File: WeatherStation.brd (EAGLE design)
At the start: 30.5 x 53.3 mm, 36 parts, among them J1 EDISON_CONNECTOR_FULLMOUNTING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, J2 EDISON_CONNECTOR_FULLHEADER, U1 MCP73831, U2 HTU21DSMD, U3 MPL3115A2LGA8, U4 PCA9306

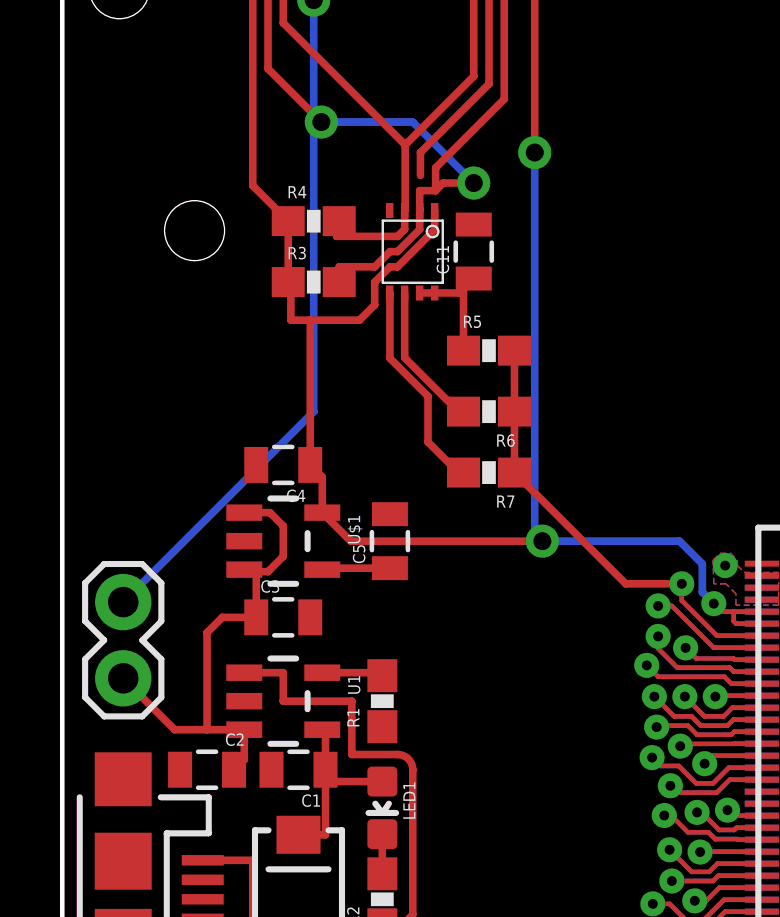
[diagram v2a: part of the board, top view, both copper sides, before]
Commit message: rearranged silkscreens
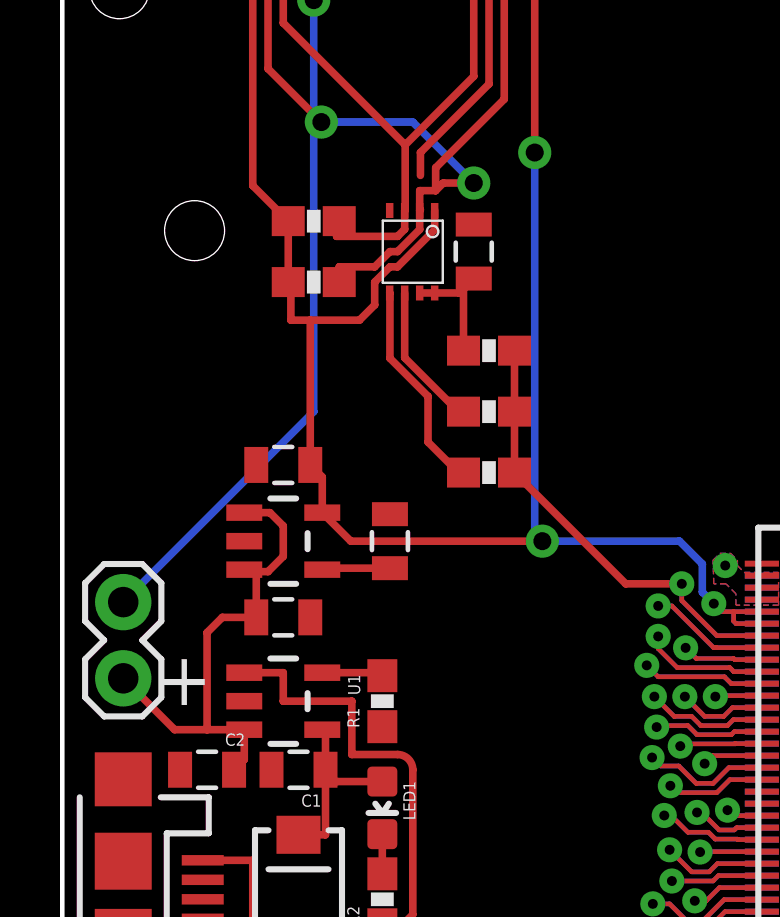
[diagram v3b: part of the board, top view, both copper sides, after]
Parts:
- U$1: value 3.3V/150mA -> MIC5205
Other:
- board text added: "+"
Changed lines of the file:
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@@
 <wire x1="11.176" y1="50.546" x2="11.176" y2="46.482" width="2.54" layer="46"/>
 <wire x1="11.176" y1="46.482" x2="9.398" y2="44.704" width="2.54" layer="46"/>
+<text x="4.064" y="19.558" size="1.778" layer="25" align="center">+</text>
 </plain>
 <attributes>
@@
 <attribute name="PROD_ID" value="IC-10023" x="11.684" y="33.782" size="1.778" layer="27" rot="R180" display="off"/>
 </element>
-<element name="U$1" library="SparkFun-PowerIC" package="SOT23-5" value="3.3V/150mA" x="7.366" y="24.13" rot="R270">
+<element name="U$1" library="SparkFun-PowerIC" package="SOT23-5" value="MIC5205" x="7.366" y="24.13" smashed="yes" rot="R270">
 <attribute name="PROD_ID" value="VREG-00822" x="7.366" y="24.13" size="1.778" layer="27" rot="R270" display="off"/>
-</element>
-<element name="C3" library="SparkFun-Capacitors" package="0805" value="4.7µF" x="7.366" y="21.59"/>
-<element name="C4" library="SparkFun-Capacitors" package="0805" value="4.7µF" x="7.366" y="26.67" rot="R180"/>
-<element name="C5" library="SparkFun-Capacitors" package="0805" value="4.7µF" x="10.922" y="24.13" rot="R90"/>
+<attribute name="VALUE" x="7.3025" y="24.1935" size="0.4064" layer="27" rot="R90" align="center"/>
+</element>
+<element name="C3" library="SparkFun-Capacitors" package="0805" value="4.7µF" x="7.366" y="21.59" smashed="yes">
+<attribute name="VALUE" x="8.89" y="21.463" size="0.4064" layer="27"/>
+</element>
+<element name="C4" library="SparkFun-Capacitors" package="0805" value="4.7µF" x="7.366" y="26.67" smashed="yes" rot="R180">
+<attribute name="VALUE" x="8.382" y="28.067" size="0.4064" layer="27" rot="R180"/>
+</element>
+<element name="C5" library="SparkFun-Capacitors" package="0805" value="4.7µF" x="10.922" y="24.13" smashed="yes" rot="R90">
+<attribute name="VALUE" x="12.319" y="23.114" size="0.4064" layer="27" rot="R90"/>
+</element>
 <element name="C6" library="SparkFun-Capacitors" package="0805" value="0.1µF" x="21.336" y="48.514" rot="R90"/>
 <element name="C7" library="SparkFun-Capacitors" package="0805" value="1µF" x="22.86" y="48.514" rot="R90"/>
-<element name="R3" library="SparkFun-Resistors" package="0603-RES" value="1kΩ" x="8.382" y="32.766"/>
-<element name="R4" library="SparkFun-Resistors" package="0603-RES" value="1kΩ" x="8.382" y="34.798"/>
-<element name="R5" library="SparkFun-Resistors" package="0603-RES" value="1kΩ" x="14.224" y="30.48"/>
-<element name="R6" library="SparkFun-Resistors" package="0603-RES" value="1kΩ" x="14.224" y="28.448" rot="R180"/>
-<element name="R7" library="SparkFun-Resistors" package="0603-RES" value="1kΩ" x="14.224" y="26.416" rot="R180"/>
+<element name="R3" library="SparkFun-Resistors" package="0603-RES" value="1kΩ" x="8.382" y="32.766" smashed="yes">
+<attribute name="VALUE" x="5.842" y="32.639" size="0.4064" layer="27"/>
+</element>
+<element name="R4" library="SparkFun-Resistors" package="0603-RES" value="1kΩ" x="8.382" y="34.798" smashed="yes">
+<attribute name="VALUE" x="5.842" y="34.671" size="0.4064" layer="27"/>
+</element>
+<element name="R5" library="SparkFun-Resistors" package="0603-RES" value="1kΩ" x="14.224" y="30.48" smashed="yes">
+<attribute name="VALUE" x="11.684" y="30.353" size="0.4064" layer="27"/>
+</element>
+<element name="R6" library="SparkFun-Resistors" package="0603-RES" value="1kΩ" x="14.224" y="28.448" smashed="yes" rot="R180">
+<attribute name="VALUE" x="11.684" y="28.321" size="0.4064" layer="27" rot="R180" align="top-right"/>
+</element>
+<element name="R7" library="SparkFun-Resistors" package="0603-RES" value="1kΩ" x="14.224" y="26.416" smashed="yes" rot="R180">
+<attribute name="VALUE" x="11.684" y="26.289" size="0.4064" layer="27"/>
+</element>
 <element name="C8" library="SparkFun-Capacitors" package="0805" value="4.7µF" x="7.112" y="51.562"/>
 <element name="C9" library="SparkFun-Capacitors" package="0805" value="0.1µF" x="17.78" y="45.72"/>
 <element name="C10" library="SparkFun-Capacitors" package="EIA3216" value="10µF" x="25.146" y="48.514" rot="R270"/>
-<element name="C11" library="SparkFun-Capacitors" package="0805" value="4.7µF" x="13.716" y="33.782" rot="R90"/>
+<element name="C11" library="SparkFun-Capacitors" package="0805" value="4.7µF" x="13.716" y="33.782" smashed="yes" rot="R90">
+<attribute name="VALUE" x="15.113" y="32.766" size="0.4064" layer="27" rot="R90"/>
+</element>
 </elements>
 <signals>

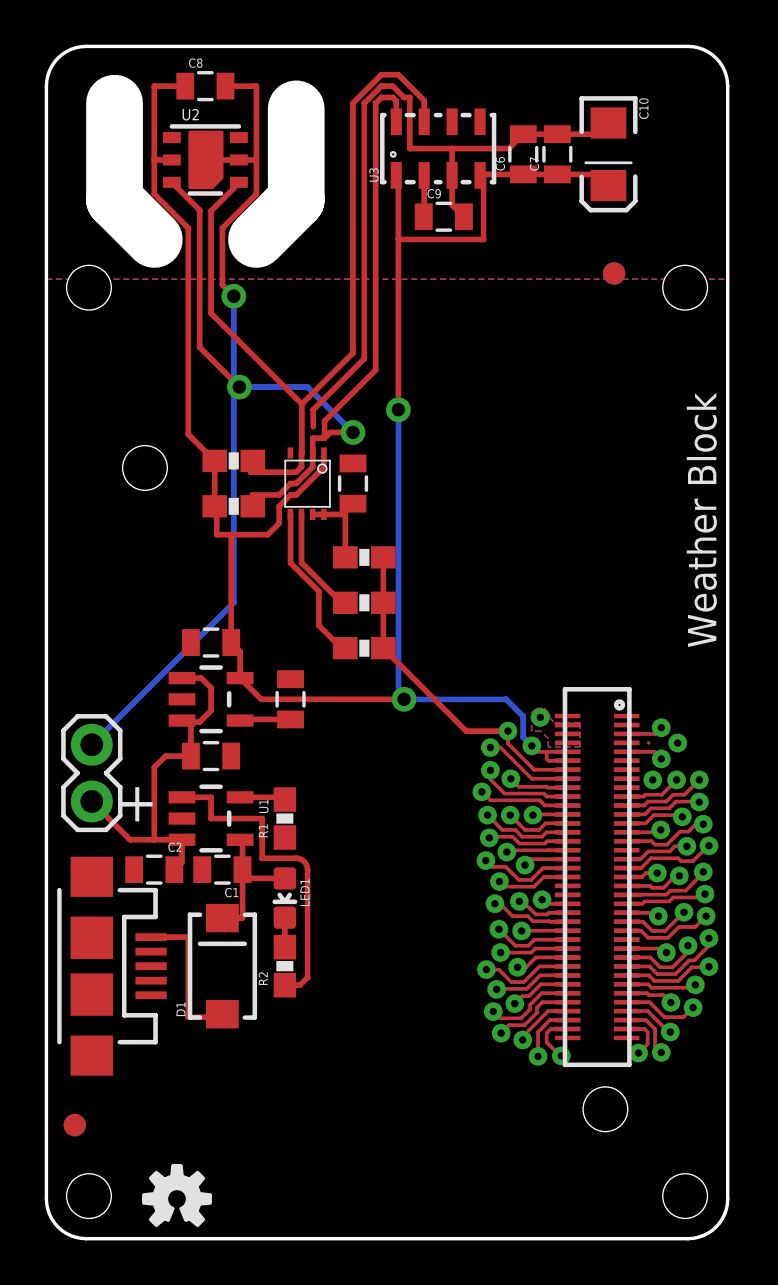
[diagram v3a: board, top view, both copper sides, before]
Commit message: rearranged silkscreens/labels
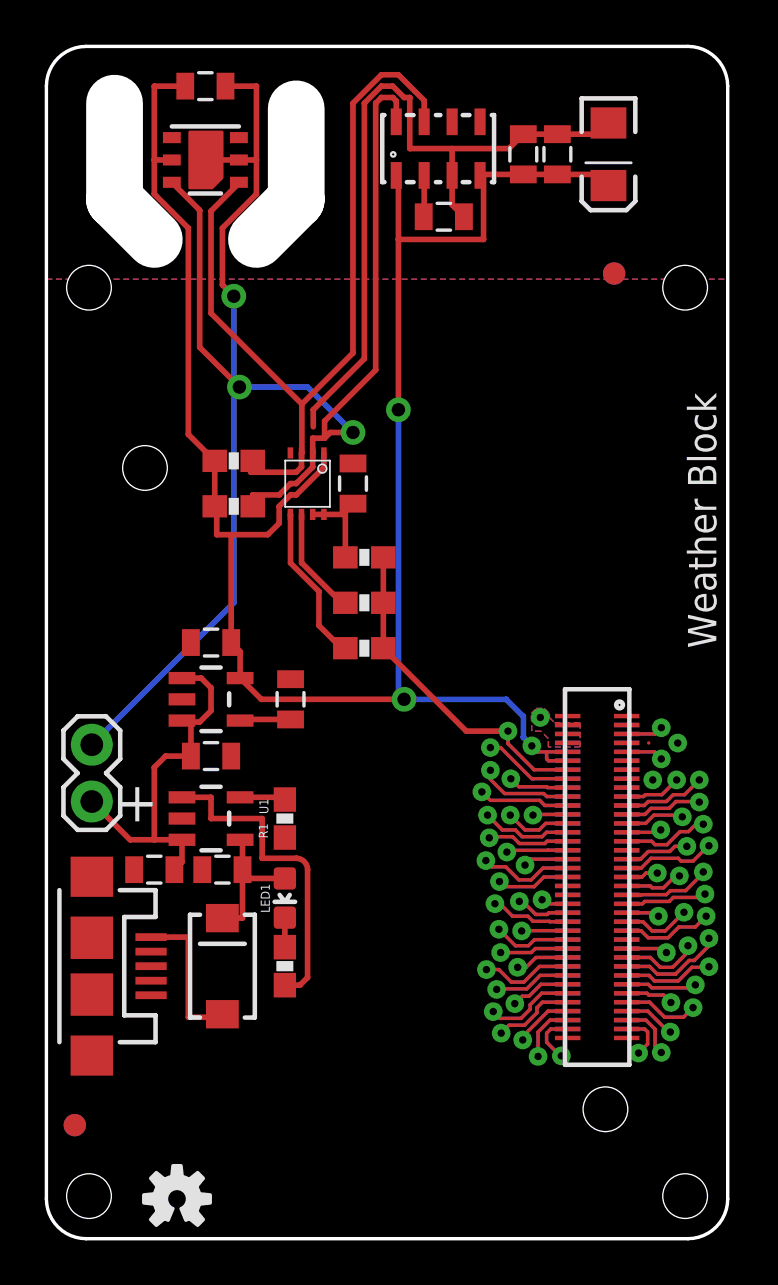
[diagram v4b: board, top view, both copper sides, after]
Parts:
- U2: value HTU21DSMD -> HTU21D
- U3: value MPL3115A2LGA8 -> MPL3115A2
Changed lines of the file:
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@@
 <dimension x1="1.778" y1="44.45" x2="5.08" y2="0" x3="38.1" y3="22.225" textsize="1.27" textratio="10" layer="51" dtype="vertical" unit="inch"/>
 <dimension x1="0" y1="53.34" x2="2.54" y2="0" x3="40.64" y3="26.67" textsize="1.27" textratio="10" layer="51" dtype="vertical" unit="inch"/>
-<rectangle x1="22.098" y1="26.162" x2="30.48" y2="44.45" layer="42" rot="R180"/>
 <rectangle x1="22.098" y1="26.162" x2="30.48" y2="44.45" layer="41" rot="R180"/>
 <dimension x1="1.905" y1="42.545" x2="0.5579625" y2="43.8920375" x3="-5.07986875" y3="49.285071875" textsize="1.27" textratio="10" layer="51" dtype="radius" unit="inch"/>
@@
 <attribute name="PROD_ID" value="CONN-09505" x="2.032" y="12.192" size="1.778" layer="27" rot="R270" display="off"/>
 </element>
-<element name="D1" library="SparkFun-DiscreteSemi" package="SMA-DIODE" value="MBRA140" x="7.874" y="12.192" rot="R90">
+<element name="D1" library="SparkFun-DiscreteSemi" package="SMA-DIODE" value="MBRA140" x="7.874" y="12.192" smashed="yes" rot="R90">
 <attribute name="PROD_ID" value="DIO-08053" x="7.874" y="12.192" size="1.778" layer="27" rot="R90" display="off"/>
 </element>
@@
 <attribute name="VALUE" x="7.4295" y="18.7325" size="0.3048" layer="27" rot="R270" align="center"/>
 </element>
-<element name="C1" library="SparkFun-Capacitors" package="0805" value="4.7µF" x="7.874" y="16.51" smashed="yes" rot="R180">
-<attribute name="NAME" x="8.636" y="15.6845" size="0.4064" layer="25" rot="R180"/>
-</element>
+<element name="C1" library="SparkFun-Capacitors" package="0805" value="4.7µF" x="7.874" y="16.51" smashed="yes" rot="R180"/>
 <element name="R1" library="SparkFun-Resistors" package="0603-RES" value="2kΩ" x="10.668" y="18.796" rot="R90"/>
 <element name="C2" library="SparkFun-Capacitors" package="0805" value="4.7µF" x="4.826" y="16.51" smashed="yes" rot="R180">
-<attribute name="NAME" x="6.096" y="17.7165" size="0.4064" layer="25" rot="R180"/>
-</element>
-<element name="LED1" library="SparkFun-LED" package="LED-0603" value="" x="10.668" y="15.24" rot="R180"/>
-<element name="R2" library="SparkFun-Resistors" package="0603-RES" value="330Ω" x="10.668" y="12.192" rot="R90"/>
+<attribute name="VALUE" x="7.112" y="15.621" size="0.4064" layer="27" rot="R180"/>
+</element>
+<element name="LED1" library="SparkFun-LED" package="LED-0603" value="" x="10.668" y="15.24" smashed="yes" rot="R180">
+<attribute name="NAME" x="9.5885" y="15.875" size="0.4064" layer="25" rot="R270"/>
+<attribute name="VALUE" x="9.5885" y="16.256" size="0.4064" layer="27" rot="R270"/>
+</element>
+<element name="R2" library="SparkFun-Resistors" package="0603-RES" value="330Ω" x="10.668" y="12.192" smashed="yes" rot="R90">
+<attribute name="VALUE" x="9.779" y="12.192" size="0.4064" layer="27" rot="R90" align="center"/>
+</element>
 <element name="JP2" library="SparkFun-Connectors" package="1X02" value="M02PTH" x="2.032" y="22.098" smashed="yes" rot="R270"/>
-<element name="U2" library="SparkFun-Sensors" package="HTU21D" value="HTU21DSMD" x="7.112" y="48.26"/>
-<element name="U3" library="SparkFun-Sensors" package="LGA8" value="MPL3115A2LGA8" x="17.526" y="48.768" rot="R90"/>
+<element name="U2" library="SparkFun-Sensors" package="HTU21D" value="HTU21D" x="7.112" y="48.26" smashed="yes">
+<attribute name="VALUE" x="5.787" y="46.06" size="0.5" layer="27"/>
+</element>
+<element name="U3" library="SparkFun-Sensors" package="LGA8" value="MPL3115A2" x="17.526" y="48.768" smashed="yes" rot="R90">
+<attribute name="VALUE" x="16.002" y="50.8" size="0.4064" layer="27" ratio="15"/>
+</element>
 <element name="U4" library="SparkFun-DigitalIC" package="PSOP-8" value="PCA9306" x="11.684" y="33.782" rot="R180">
 <attribute name="PROD_ID" value="IC-10023" x="11.684" y="33.782" size="1.778" layer="27" rot="R180" display="off"/>
@@
 </element>
 <element name="C5" library="SparkFun-Capacitors" package="0805" value="4.7µF" x="10.922" y="24.13" smashed="yes" rot="R90">
-<attribute name="VALUE" x="12.319" y="23.114" size="0.4064" layer="27" rot="R90"/>
-</element>
-<element name="C6" library="SparkFun-Capacitors" package="0805" value="0.1µF" x="21.336" y="48.514" rot="R90"/>
-<element name="C7" library="SparkFun-Capacitors" package="0805" value="1µF" x="22.86" y="48.514" rot="R90"/>
+<attribute name="VALUE" x="11.811" y="24.13" size="0.4064" layer="27" rot="R90" align="top-center"/>
+</element>
+<element name="C6" library="SparkFun-Capacitors" package="0805" value="0.1µF" x="21.336" y="48.514" smashed="yes" rot="R90">
+<attribute name="VALUE" x="21.463" y="46.99" size="0.4064" layer="27" rot="R90" align="bottom-right"/>
+</element>
+<element name="C7" library="SparkFun-Capacitors" package="0805" value="1µF" x="22.86" y="48.514" smashed="yes" rot="R90">
+<attribute name="VALUE" x="22.987" y="46.99" size="0.4064" layer="27" rot="R90" align="bottom-right"/>
+</element>
 <element name="R3" library="SparkFun-Resistors" package="0603-RES" value="1kΩ" x="8.382" y="32.766" smashed="yes">
 <attribute name="VALUE" x="5.842" y="32.639" size="0.4064" layer="27"/>
@@
 <attribute name="VALUE" x="11.684" y="26.289" size="0.4064" layer="27"/>
 </element>
-<element name="C8" library="SparkFun-Capacitors" package="0805" value="4.7µF" x="7.112" y="51.562"/>
-<element name="C9" library="SparkFun-Capacitors" package="0805" value="0.1µF" x="17.78" y="45.72"/>
-<element name="C10" library="SparkFun-Capacitors" package="EIA3216" value="10µF" x="25.146" y="48.514" rot="R270"/>
+<element name="C8" library="SparkFun-Capacitors" package="0805" value="4.7µF" x="7.112" y="51.562" smashed="yes">
+<attribute name="VALUE" x="7.112" y="50.673" size="0.4064" layer="27" align="top-center"/>
+</element>
+<element name="C9" library="SparkFun-Capacitors" package="0805" value="0.1µF" x="17.78" y="45.72" smashed="yes">
+<attribute name="VALUE" x="16.764" y="44.323" size="0.4064" layer="27"/>
+</element>
+<element name="C10" library="SparkFun-Capacitors" package="EIA3216" value="10µF" x="25.146" y="48.514" smashed="yes" rot="R270">
+<attribute name="VALUE" x="26.478" y="48.106" size="0.4064" layer="27" rot="R270"/>
+</element>
 <element name="C11" library="SparkFun-Capacitors" package="0805" value="4.7µF" x="13.716" y="33.782" smashed="yes" rot="R90">
 <attribute name="VALUE" x="15.113" y="32.766" size="0.4064" layer="27" rot="R90"/>
